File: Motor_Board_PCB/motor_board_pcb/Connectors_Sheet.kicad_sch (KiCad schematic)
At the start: 10 parts, among them J10 Conn_02x03_Counter_Clockwise, J11 CSP-USC16-TR, J8 Conn_01x02

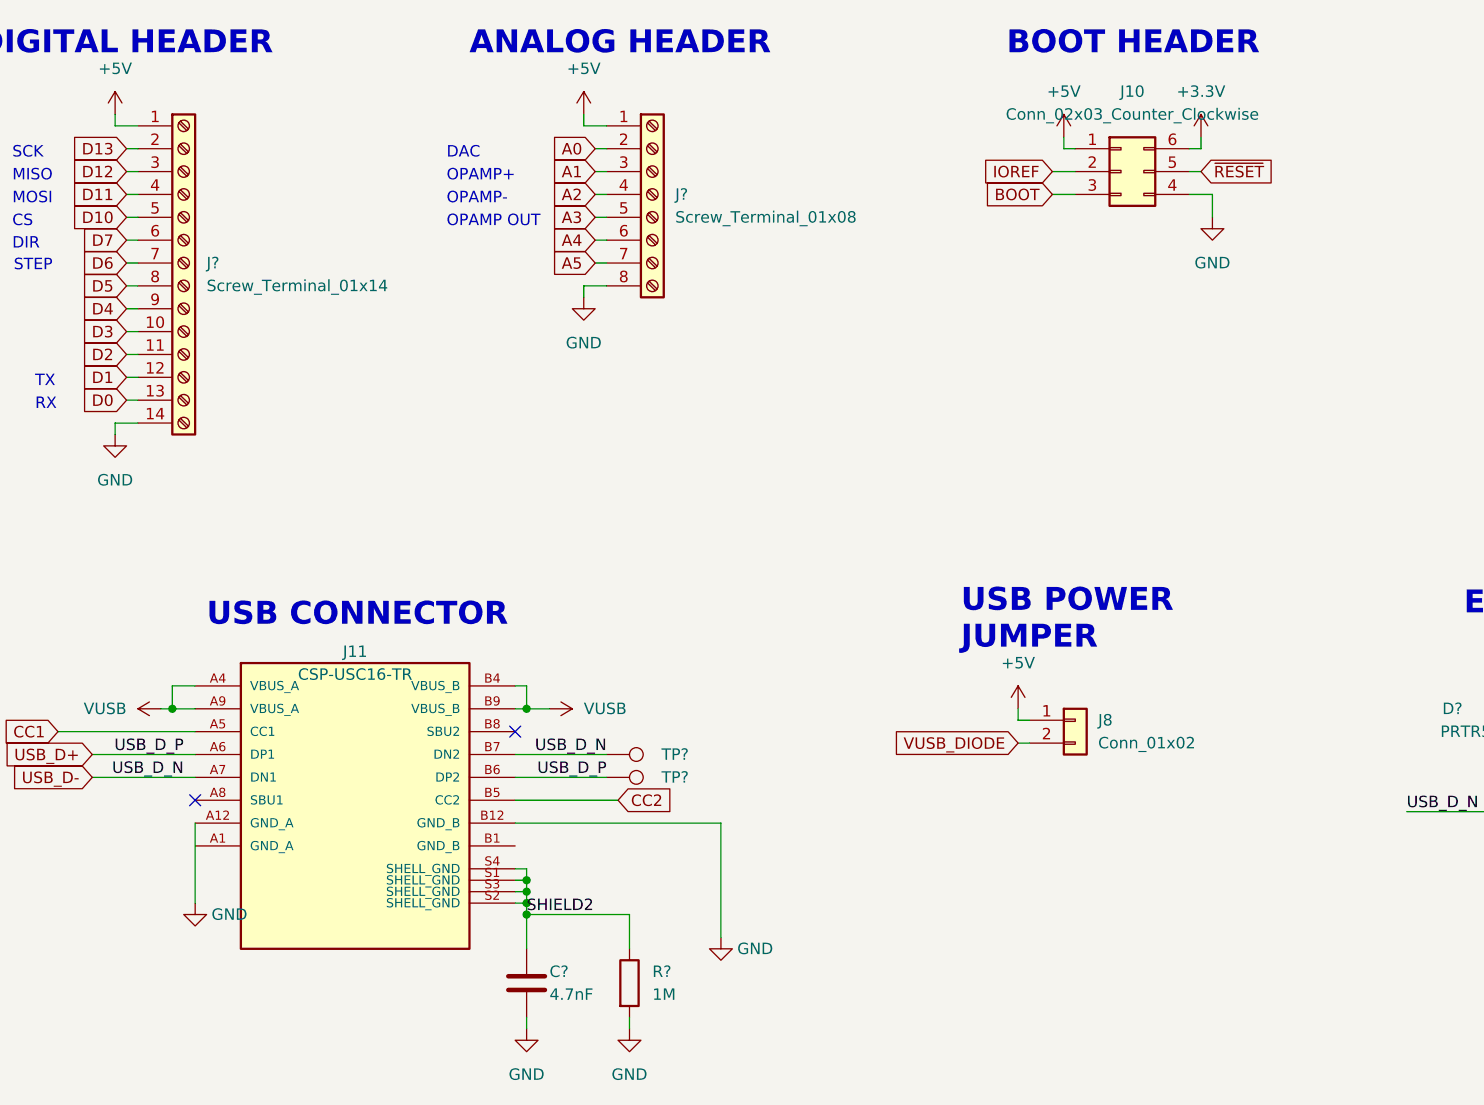
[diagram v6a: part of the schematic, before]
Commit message: - fixed capacitor values on MCU sheet (both central hub and motor board) - added missing Accelerometer componenets - changed BOOT HEADER (both central hub and motor board) - set the Arduino "love" signal to NC - fixed overlapping pins on USB connector
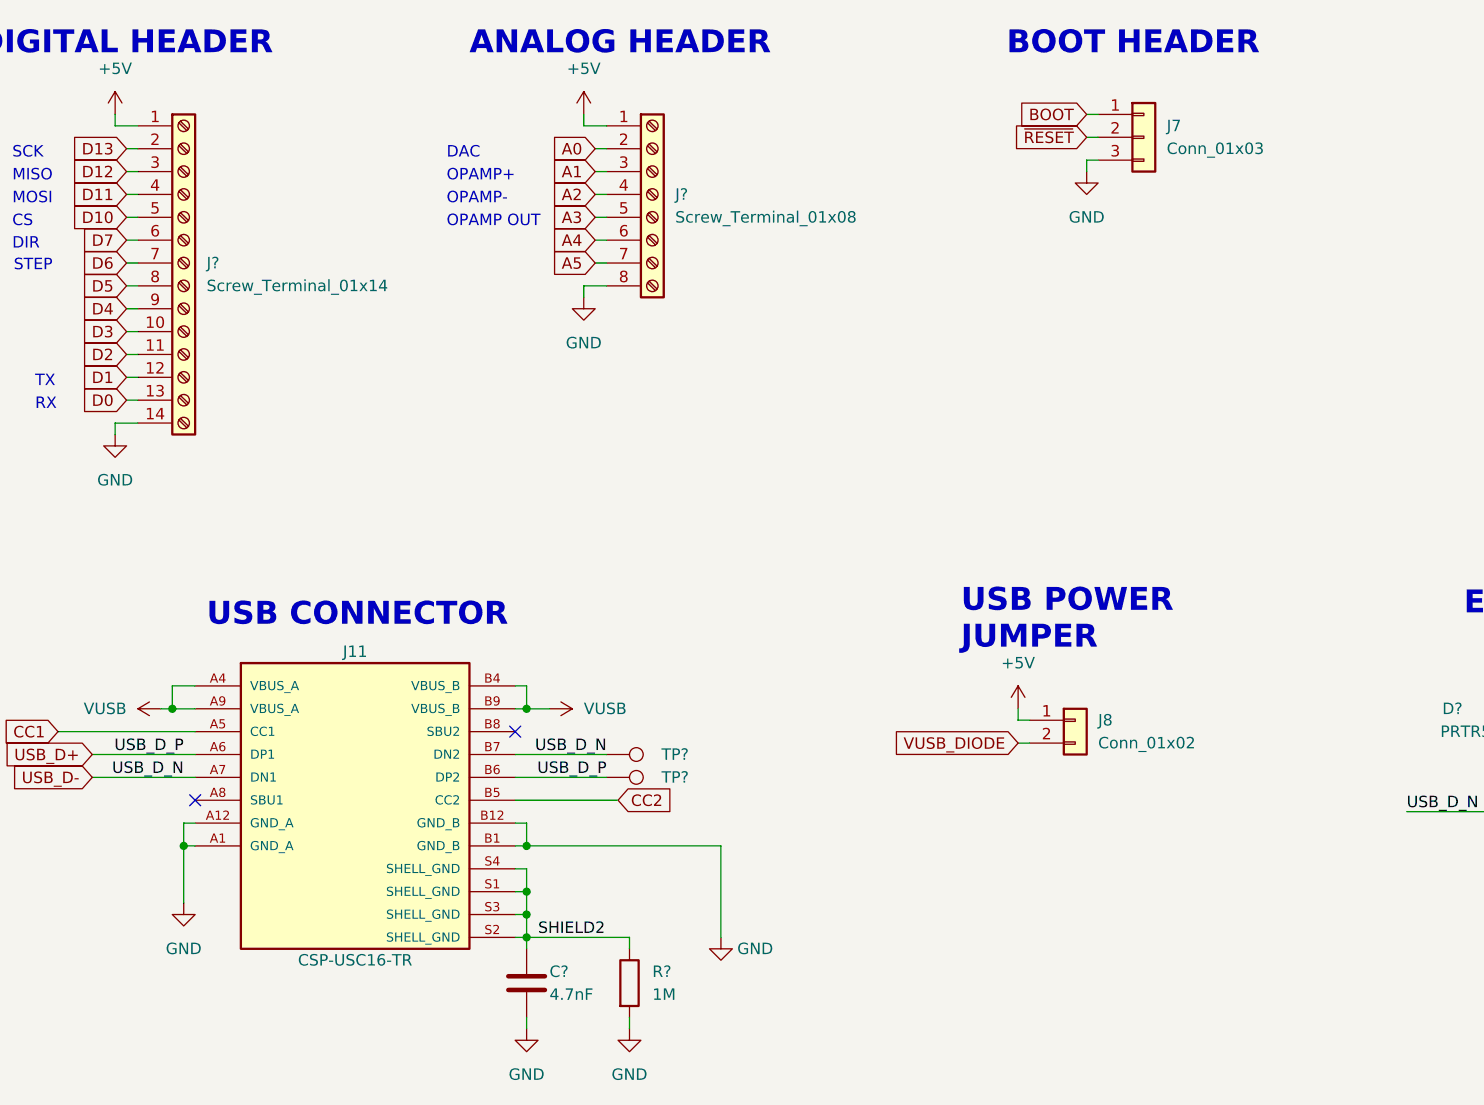
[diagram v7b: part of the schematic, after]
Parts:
- removed J10: Conn_02x03_Counter_Clockwise, Connector_PinHeader_2.54mm:PinHeader_2x03_P2.54mm_Vertical, symbol Connector_Generic:Conn_02x03_Counter_Clockwise
- added J7: Conn_01x03, Connector_PinHeader_2.54mm:PinHeader_1x03_P2.54mm_Vertical, symbol Connector_Generic:Conn_01x03
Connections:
- net BOOT: now also J7.1 (Pin_1)
- net GND: now also J11.A1 (GND_A), J11.B1 (GND_B), J7.3 (Pin_3)
- net ~{RESET}: now also J7.2 (Pin_2)

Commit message: Schematic changes before sending to kim
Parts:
- removed J?: Screw_Terminal_01x08, Connector_PinHeader_2.54mm:PinHeader_1x08_P2.54mm_Vertical, symbol Connector:Screw_Terminal_01x08
- added J6: Screw_Terminal_01x04, Connector_PinHeader_2.54mm:PinHeader_1x04_P2.54mm_Vertical, symbol Connector:Screw_Terminal_01x04
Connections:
- net A0: now also J6.4
- net A1: now also J6.1
- net A2: now also J6.2
- net A3: now also J6.3
